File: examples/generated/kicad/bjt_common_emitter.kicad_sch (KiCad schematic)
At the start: 6 parts, among them Q1 2N3904

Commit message: Attempt to create legible symbols.
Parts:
- Q1: symbol examples:QNPN -> QNPN
- RB, RC, RE: symbol examples:R -> R
- VCC, VIN: symbol examples:VSOURCE -> VSOURCE
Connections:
- net GND: now also RB.1, RC.1, RE.2, VCC.1 (E1), VCC.2 (E2), VIN.1 (E1)
- new net: Q1.2 (B), RB.2
- new net: Q1.1 (C), RE.1
- new net: Q1.3 (E), RC.2
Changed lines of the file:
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@@
     (comment 1 "Generated by mixedsig2cad")
   )
-  (symbol (lib_id "examples:VSOURCE") (at 50.00 55.00 0) (unit 1)
+  (symbol (lib_id "VSOURCE") (at 50.00 55.00 0) (unit 1)
     (in_bom yes) (on_board yes)
     (property "Reference" "VCC" (at 50.0 51.19 0)
@@
     )
   )
-  (symbol (lib_id "examples:VSOURCE") (at 50.00 90.00 0) (unit 1)
+  (symbol (lib_id "VSOURCE") (at 50.00 90.00 0) (unit 1)
     (in_bom yes) (on_board yes)
     (property "Reference" "VIN" (at 50.0 86.19 0)
@@
     )
   )
-  (symbol (lib_id "examples:R") (at 95.00 55.00 90) (unit 1)
+  (symbol (lib_id "R") (at 95.00 55.00 90) (unit 1)
     (in_bom yes) (on_board yes)
     (property "Reference" "RB" (at 95.0 51.19 0)
@@
     )
   )
-  (symbol (lib_id "examples:R") (at 95.00 90.00 90) (unit 1)
+  (symbol (lib_id "R") (at 95.00 90.00 90) (unit 1)
     (in_bom yes) (on_board yes)
     (property "Reference" "RC" (at 95.0 86.19 0)
@@
     )
   )
-  (symbol (lib_id "examples:R") (at 95.00 125.00 90) (unit 1)
+  (symbol (lib_id "R") (at 95.00 125.00 90) (unit 1)
     (in_bom yes) (on_board yes)
     (property "Reference" "RE" (at 95.0 121.19 0)
@@
     )
   )
-  (symbol (lib_id "examples:QNPN") (at 150.00 85.00 0) (unit 1)
+  (symbol (lib_id "QNPN") (at 150.00 85.00 0) (unit 1)
     (in_bom yes) (on_board yes)
     (property "Reference" "Q1" (at 150.0 81.19 0)
@@
     )
   )
-  (symbol (lib_id "examples:GND") (at 38.00 41.38 0) (unit 1)
+  (symbol (lib_id "GND") (at 38.00 41.38 0) (unit 1)
     (in_bom yes) (on_board yes)
     (property "Reference" "#PWR0001" (at 38.0 37.57 0)
@@
     )
   )
-  (symbol (lib_id "examples:VCC") (at 38.00 49.00 0) (unit 1)
+  (symbol (lib_id "VCC") (at 38.00 49.00 0) (unit 1)
     (in_bom yes) (on_board yes)
     (property "Reference" "#PWR0002" (at 38.0 45.19 0)

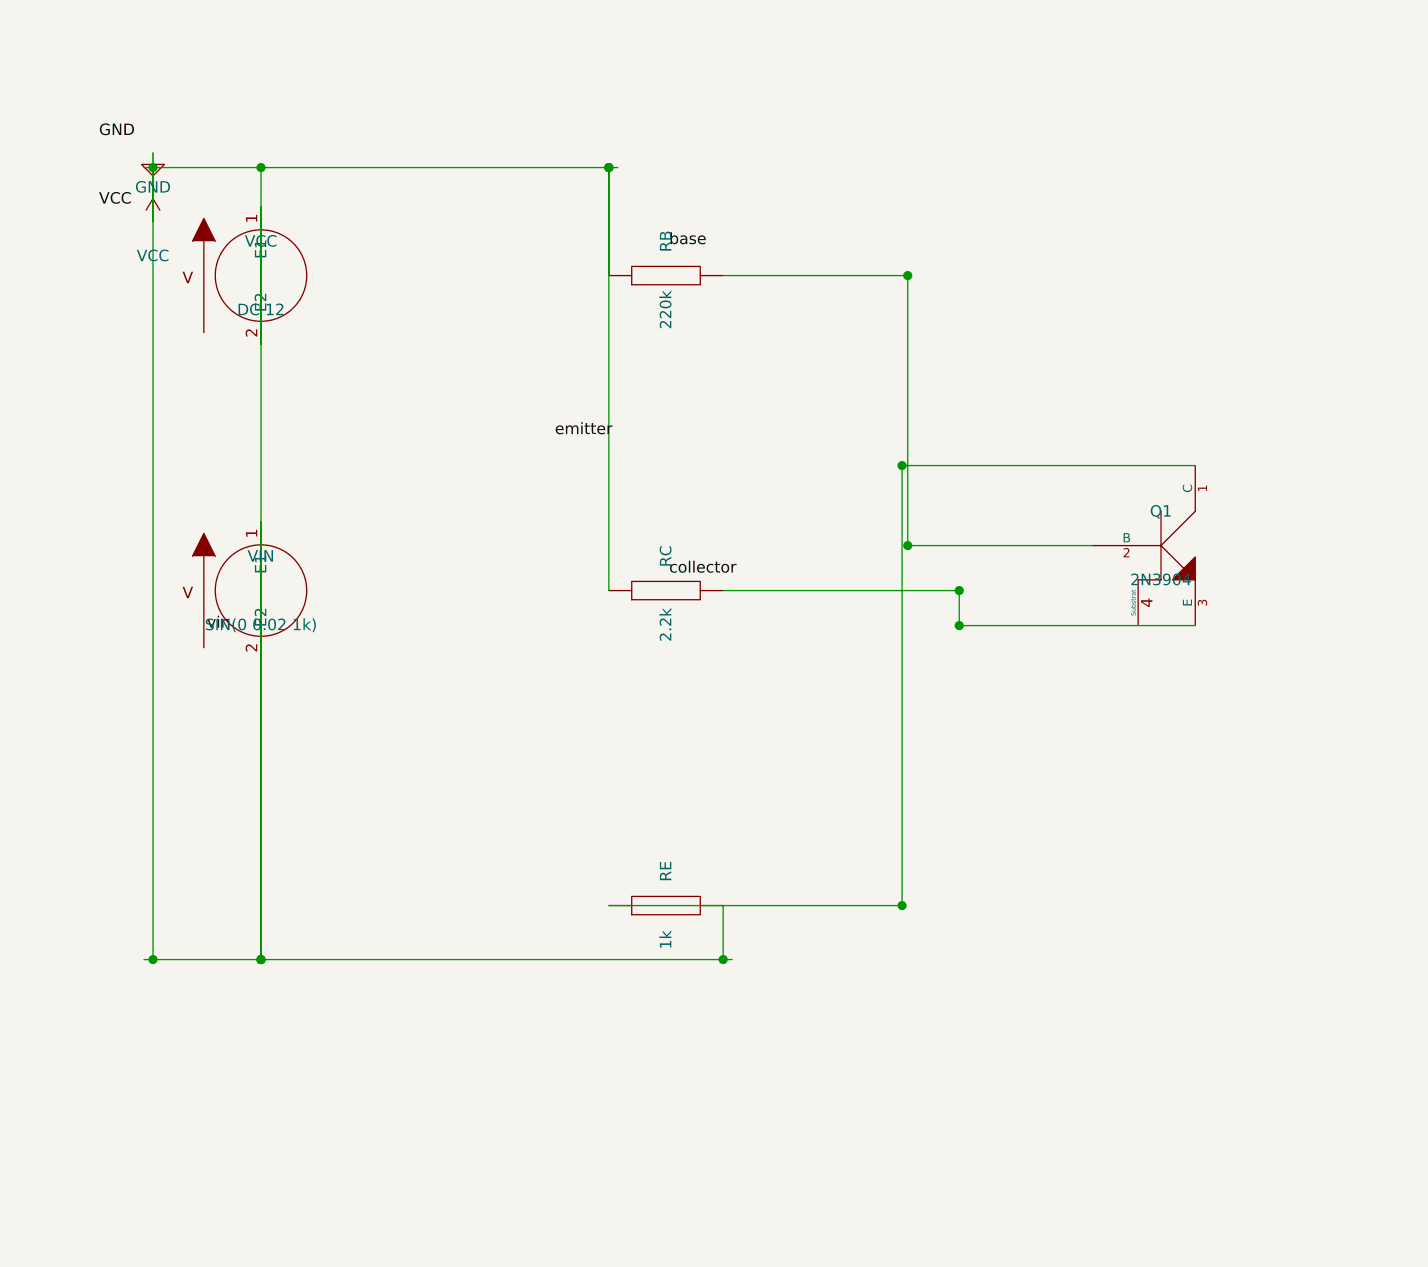
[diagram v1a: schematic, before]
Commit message: Attempt full seperation of circuit concerns into layers.
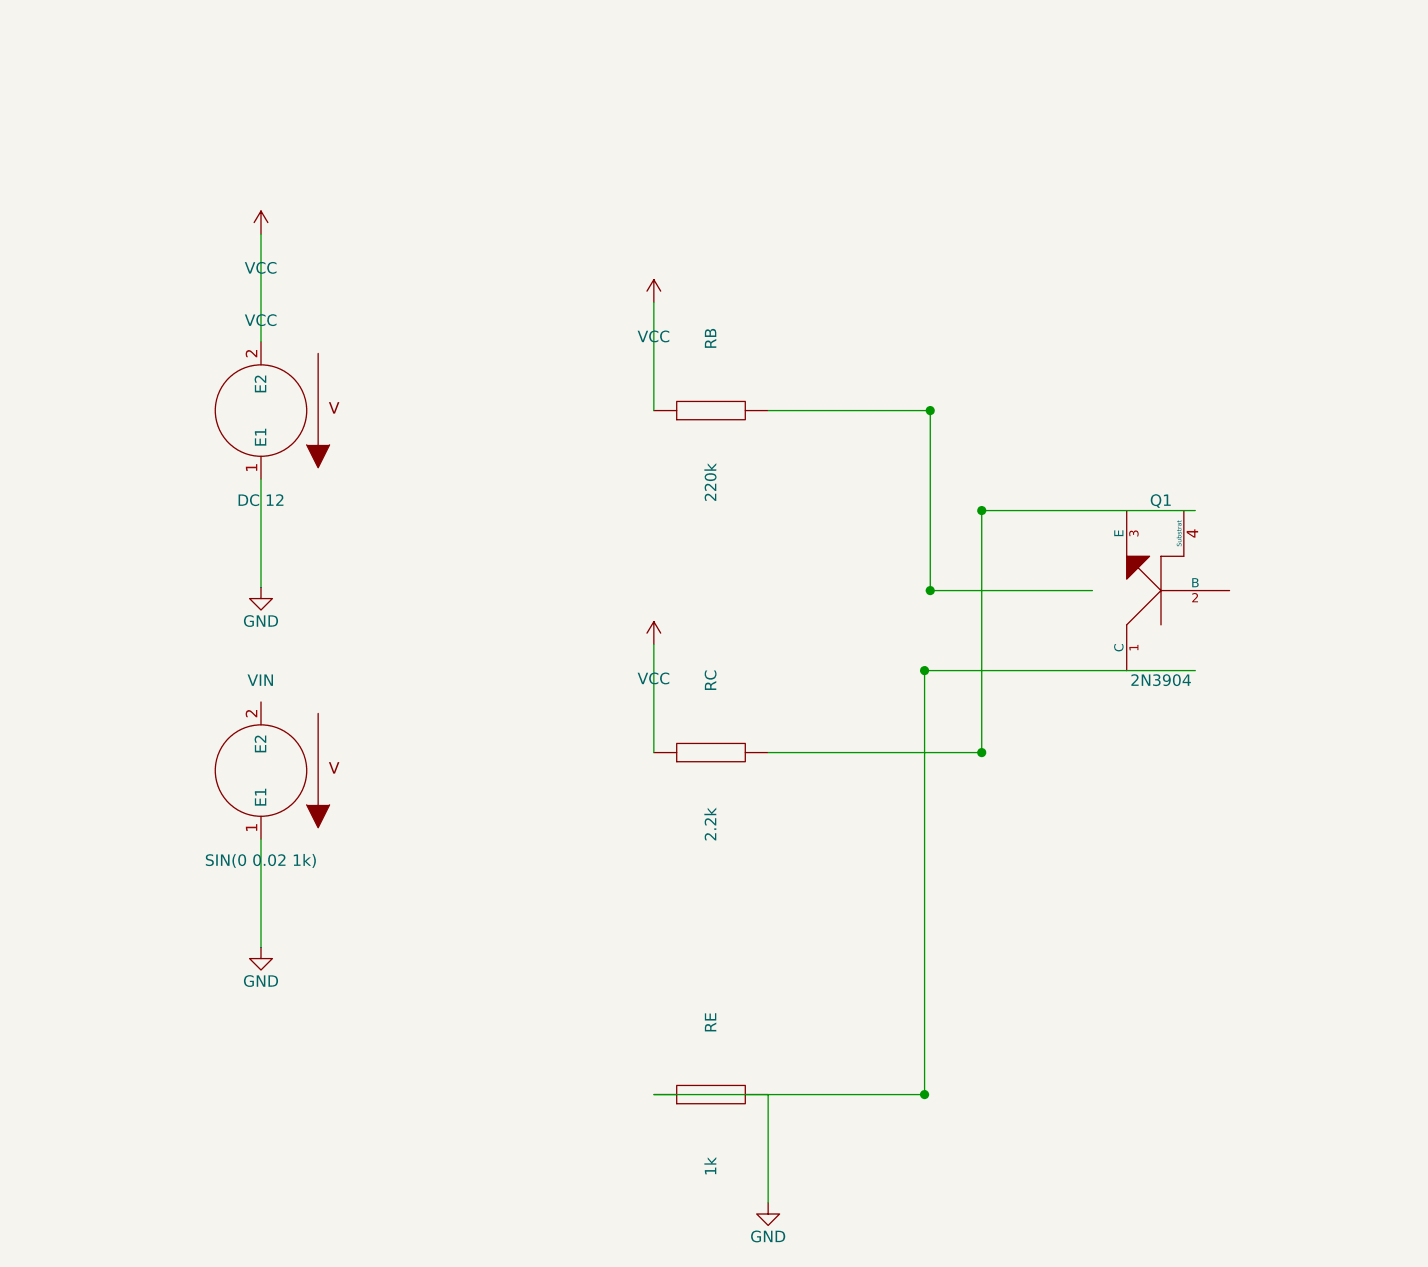
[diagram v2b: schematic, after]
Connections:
- net GND: no longer RB.1, RC.1, VCC.2 (E2)
- net at RB.2: no longer Q1.2 (B)
- net at RE.1: no longer Q1.1 (C)
- net at Q1.3 (E): no longer RC.2
- new net VCC: RB.1, RC.1, VCC.2 (E2)
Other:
- moved on the sheet: Q1, RB, RC, RE, VCC, VIN

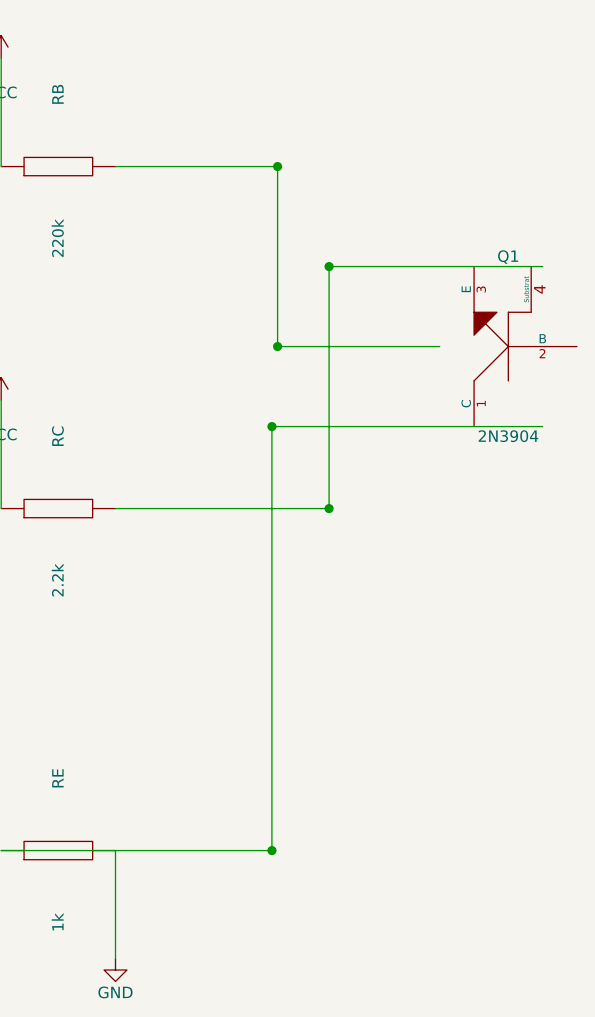
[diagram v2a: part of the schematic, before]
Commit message: Add checks for connectivity.
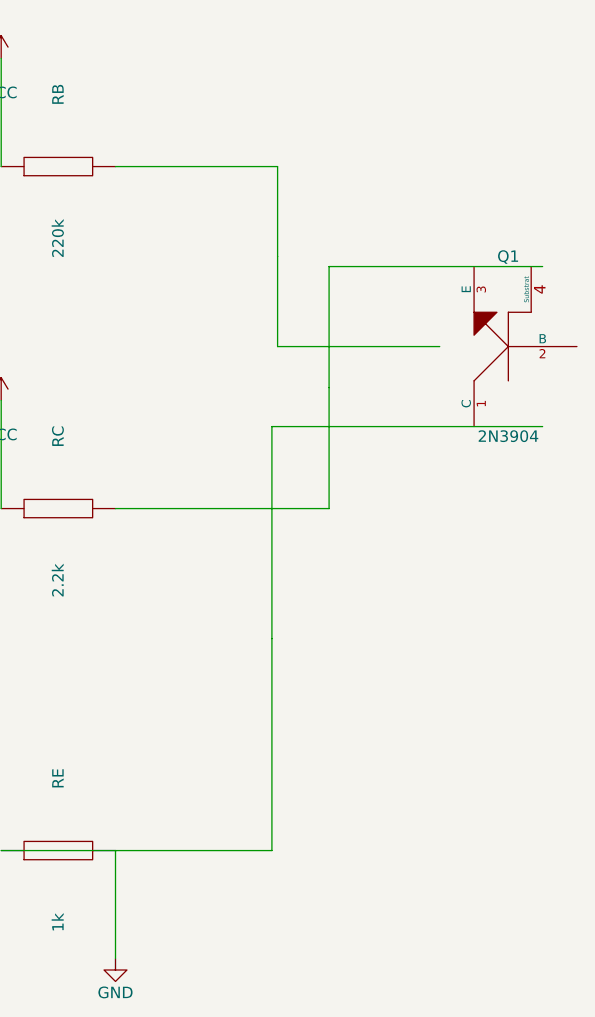
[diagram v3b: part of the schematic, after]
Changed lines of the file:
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@@
     (stroke (width 0) (type solid) (color 0 0 0 0))
   )
-  (wire (pts (xy 124.36 70.00) (xy 124.36 90.00))
+  (wire (pts (xy 124.36 70.00) (xy 124.36 80.00))
     (stroke (width 0) (type solid) (color 0 0 0 0))
   )
-  (wire (pts (xy 124.36 90.00) (xy 142.38 90.00))
+  (wire (pts (xy 142.38 90.00) (xy 124.36 90.00))
+    (stroke (width 0) (type solid) (color 0 0 0 0))
+  )
+  (wire (pts (xy 124.36 90.00) (xy 124.36 80.00))
     (stroke (width 0) (type solid) (color 0 0 0 0))
   )
@@
     (stroke (width 0) (type solid) (color 0 0 0 0))
   )
-  (wire (pts (xy 130.08 108.00) (xy 130.08 81.11))
+  (wire (pts (xy 130.08 108.00) (xy 130.08 94.56))
     (stroke (width 0) (type solid) (color 0 0 0 0))
   )
-  (wire (pts (xy 130.08 81.11) (xy 153.81 81.11))
+  (wire (pts (xy 153.81 81.11) (xy 130.08 81.11))
+    (stroke (width 0) (type solid) (color 0 0 0 0))
+  )
+  (wire (pts (xy 130.08 81.11) (xy 130.08 94.56))
     (stroke (width 0) (type solid) (color 0 0 0 0))
   )
@@
     (stroke (width 0) (type solid) (color 0 0 0 0))
   )
-  (wire (pts (xy 123.73 146.00) (xy 123.73 98.89))
+  (wire (pts (xy 123.73 146.00) (xy 123.73 122.44))
     (stroke (width 0) (type solid) (color 0 0 0 0))
   )
-  (wire (pts (xy 123.73 98.89) (xy 153.81 98.89))
+  (wire (pts (xy 153.81 98.89) (xy 123.73 98.89))
     (stroke (width 0) (type solid) (color 0 0 0 0))
   )
-  (junction (at 124.36 70.00) (diameter 1.016) (color 0 0 0 0))
-  (junction (at 124.36 90.00) (diameter 1.016) (color 0 0 0 0))
-  (junction (at 130.08 108.00) (diameter 1.016) (color 0 0 0 0))
-  (junction (at 130.08 81.11) (diameter 1.016) (color 0 0 0 0))
-  (junction (at 123.73 146.00) (diameter 1.016) (color 0 0 0 0))
-  (junction (at 123.73 98.89) (diameter 1.016) (color 0 0 0 0))
+  (wire (pts (xy 123.73 98.89) (xy 123.73 122.44))
+    (stroke (width 0) (type solid) (color 0 0 0 0))
+  )
   (sheet_instances
     (path "/" (page "1"))

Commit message: Attempt to correct strange wiring.
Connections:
- net at RE.1: now also RC.2
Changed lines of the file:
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@@
     (stroke (width 0) (type solid) (color 0 0 0 0))
   )
-  (wire (pts (xy 106.35 70.00) (xy 124.36 70.00))
+  (wire (pts (xy 106.35 70.00) (xy 108.50 70.00))
     (stroke (width 0) (type solid) (color 0 0 0 0))
   )
-  (wire (pts (xy 124.36 70.00) (xy 124.36 80.00))
+  (wire (pts (xy 108.50 70.00) (xy 108.50 90.00))
     (stroke (width 0) (type solid) (color 0 0 0 0))
   )
-  (wire (pts (xy 142.38 90.00) (xy 124.36 90.00))
+  (wire (pts (xy 108.50 90.00) (xy 142.38 90.00))
     (stroke (width 0) (type solid) (color 0 0 0 0))
   )
-  (wire (pts (xy 124.36 90.00) (xy 124.36 80.00))
+  (wire (pts (xy 106.35 108.00) (xy 153.81 108.00))
     (stroke (width 0) (type solid) (color 0 0 0 0))
   )
-  (wire (pts (xy 106.35 108.00) (xy 130.08 108.00))
+  (wire (pts (xy 153.81 108.00) (xy 153.81 81.11))
     (stroke (width 0) (type solid) (color 0 0 0 0))
   )
-  (wire (pts (xy 130.08 108.00) (xy 130.08 94.56))
+  (wire (pts (xy 93.65 146.00) (xy 153.81 146.00))
     (stroke (width 0) (type solid) (color 0 0 0 0))
   )
-  (wire (pts (xy 153.81 81.11) (xy 130.08 81.11))
+  (wire (pts (xy 153.81 146.00) (xy 153.81 98.89))
     (stroke (width 0) (type solid) (color 0 0 0 0))
   )
-  (wire (pts (xy 130.08 81.11) (xy 130.08 94.56))
-    (stroke (width 0) (type solid) (color 0 0 0 0))
-  )
-  (wire (pts (xy 93.65 146.00) (xy 123.73 146.00))
-    (stroke (width 0) (type solid) (color 0 0 0 0))
-  )
-  (wire (pts (xy 123.73 146.00) (xy 123.73 122.44))
-    (stroke (width 0) (type solid) (color 0 0 0 0))
-  )
-  (wire (pts (xy 153.81 98.89) (xy 123.73 98.89))
-    (stroke (width 0) (type solid) (color 0 0 0 0))
-  )
-  (wire (pts (xy 123.73 98.89) (xy 123.73 122.44))
-    (stroke (width 0) (type solid) (color 0 0 0 0))
-  )

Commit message: Attempt shape and wiring fixes again.
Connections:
- net VCC: now also RE.1
- net at RB.2: now also RC.2
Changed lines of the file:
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@@
     )
   )
-  (wire (pts (xy 50.00 62.38) (xy 50.00 50.38))
+  (wire (pts (xy 50.00 62.38) (xy 50.00 60.50))
     (stroke (width 0) (type solid) (color 0 0 0 0))
   )
-  (wire (pts (xy 50.00 77.62) (xy 50.00 89.62))
+  (wire (pts (xy 50.00 60.50) (xy 56.00 60.50))
     (stroke (width 0) (type solid) (color 0 0 0 0))
   )
-  (wire (pts (xy 50.00 117.62) (xy 50.00 129.62))
+  (wire (pts (xy 56.00 60.50) (xy 56.00 50.38))
     (stroke (width 0) (type solid) (color 0 0 0 0))
   )
-  (wire (pts (xy 93.65 70.00) (xy 93.65 58.00))
+  (wire (pts (xy 56.00 50.38) (xy 50.00 50.38))
     (stroke (width 0) (type solid) (color 0 0 0 0))
   )
-  (wire (pts (xy 93.65 108.00) (xy 93.65 96.00))
+  (wire (pts (xy 50.00 77.62) (xy 50.00 79.50))
     (stroke (width 0) (type solid) (color 0 0 0 0))
   )
-  (wire (pts (xy 106.35 146.00) (xy 106.35 158.00))
+  (wire (pts (xy 50.00 79.50) (xy 56.00 79.50))
+    (stroke (width 0) (type solid) (color 0 0 0 0))
+  )
+  (wire (pts (xy 56.00 79.50) (xy 56.00 89.62))
+    (stroke (width 0) (type solid) (color 0 0 0 0))
+  )
+  (wire (pts (xy 56.00 89.62) (xy 50.00 89.62))
+    (stroke (width 0) (type solid) (color 0 0 0 0))
+  )
+  (wire (pts (xy 50.00 117.62) (xy 50.00 119.50))
+    (stroke (width 0) (type solid) (color 0 0 0 0))
+  )
+  (wire (pts (xy 50.00 119.50) (xy 56.00 119.50))
+    (stroke (width 0) (type solid) (color 0 0 0 0))
+  )
+  (wire (pts (xy 56.00 119.50) (xy 56.00 129.62))
+    (stroke (width 0) (type solid) (color 0 0 0 0))
+  )
+  (wire (pts (xy 56.00 129.62) (xy 50.00 129.62))
+    (stroke (width 0) (type solid) (color 0 0 0 0))
+  )
+  (wire (pts (xy 93.65 70.00) (xy 91.50 70.00))
+    (stroke (width 0) (type solid) (color 0 0 0 0))
+  )
+  (wire (pts (xy 91.50 70.00) (xy 91.50 65.00))
+    (stroke (width 0) (type solid) (color 0 0 0 0))
+  )
+  (wire (pts (xy 91.50 65.00) (xy 99.65 65.00))
+    (stroke (width 0) (type solid) (color 0 0 0 0))
+  )
+  (wire (pts (xy 99.65 65.00) (xy 99.65 58.00))
+    (stroke (width 0) (type solid) (color 0 0 0 0))
+  )
+  (wire (pts (xy 99.65 58.00) (xy 93.65 58.00))
+    (stroke (width 0) (type solid) (color 0 0 0 0))
+  )
+  (wire (pts (xy 93.65 108.00) (xy 91.50 108.00))
+    (stroke (width 0) (type solid) (color 0 0 0 0))
+  )
+  (wire (pts (xy 91.50 108.00) (xy 91.50 103.00))
+    (stroke (width 0) (type solid) (color 0 0 0 0))
+  )
+  (wire (pts (xy 91.50 103.00) (xy 99.65 103.00))
+    (stroke (width 0) (type solid) (color 0 0 0 0))
+  )
+  (wire (pts (xy 99.65 103.00) (xy 99.65 96.00))
+    (stroke (width 0) (type solid) (color 0 0 0 0))
+  )
+  (wire (pts (xy 99.65 96.00) (xy 93.65 96.00))
+    (stroke (width 0) (type solid) (color 0 0 0 0))
+  )
+  (wire (pts (xy 106.35 146.00) (xy 112.35 146.00))
+    (stroke (width 0) (type solid) (color 0 0 0 0))
+  )
+  (wire (pts (xy 112.35 146.00) (xy 112.35 158.00))
+    (stroke (width 0) (type solid) (color 0 0 0 0))
+  )
+  (wire (pts (xy 112.35 158.00) (xy 106.35 158.00))
     (stroke (width 0) (type solid) (color 0 0 0 0))
   )
@@
     (stroke (width 0) (type solid) (color 0 0 0 0))
   )
-  (wire (pts (xy 106.35 108.00) (xy 153.81 108.00))
+  (wire (pts (xy 106.35 108.00) (xy 108.50 108.00))
     (stroke (width 0) (type solid) (color 0 0 0 0))
   )
-  (wire (pts (xy 153.81 108.00) (xy 153.81 81.11))
+  (wire (pts (xy 108.50 108.00) (xy 108.50 81.00))
     (stroke (width 0) (type solid) (color 0 0 0 0))
   )
-  (wire (pts (xy 93.65 146.00) (xy 153.81 146.00))
+  (wire (pts (xy 108.50 81.00) (xy 153.81 81.00))
     (stroke (width 0) (type solid) (color 0 0 0 0))
   )
-  (wire (pts (xy 153.81 146.00) (xy 153.81 98.89))
+  (wire (pts (xy 153.81 81.00) (xy 153.81 81.11))
     (stroke (width 0) (type solid) (color 0 0 0 0))
   )
+  (wire (pts (xy 93.65 146.00) (xy 91.50 146.00))
+    (stroke (width 0) (type solid) (color 0 0 0 0))
+  )
+  (wire (pts (xy 91.50 146.00) (xy 91.50 99.00))
+    (stroke (width 0) (type solid) (color 0 0 0 0))
+  )
+  (wire (pts (xy 91.50 99.00) (xy 153.81 99.00))
+    (stroke (width 0) (type solid) (color 0 0 0 0))
+  )
+  (wire (pts (xy 153.81 99.00) (xy 153.81 98.89))
+    (stroke (width 0) (type solid) (color 0 0 0 0))
+  )
